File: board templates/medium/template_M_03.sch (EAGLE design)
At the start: 2 parts

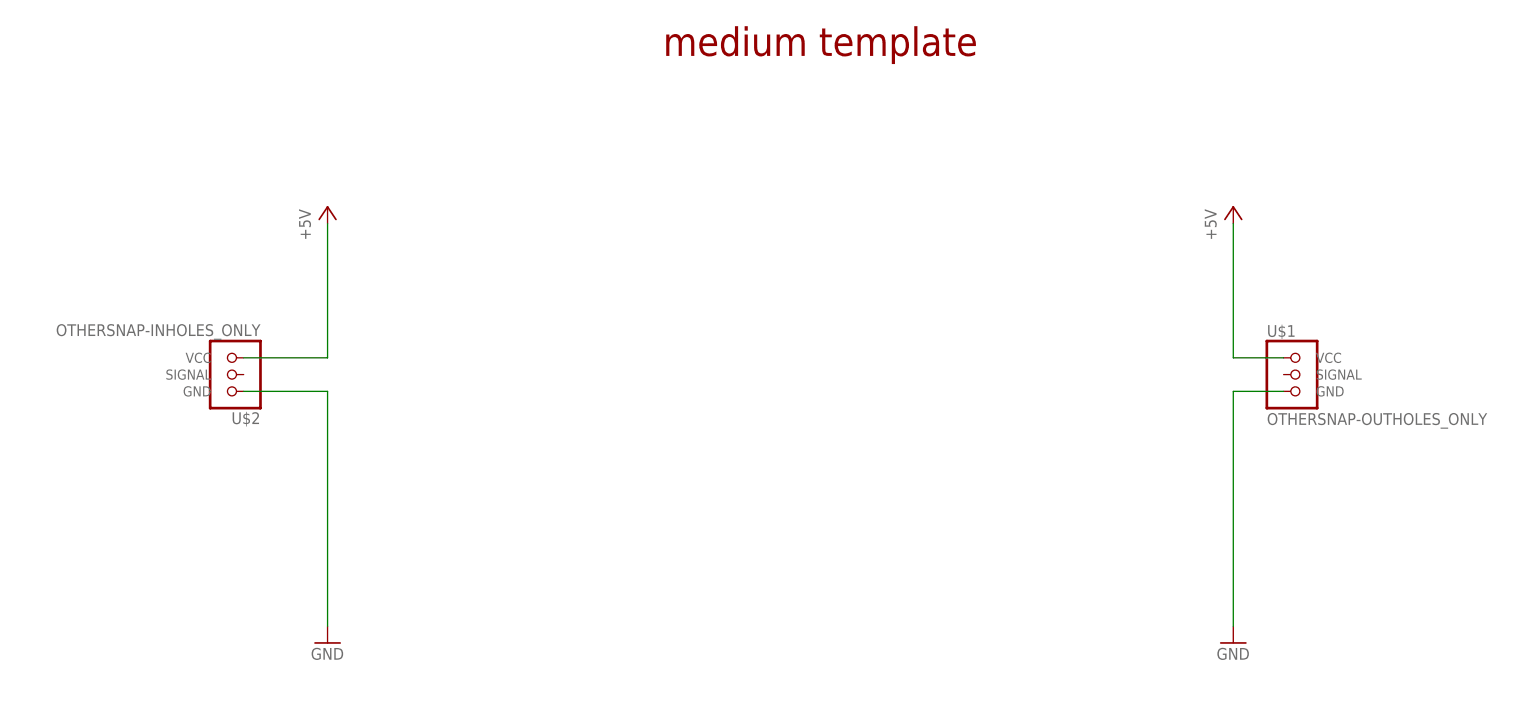
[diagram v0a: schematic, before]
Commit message: standard grid sizes on brd templates
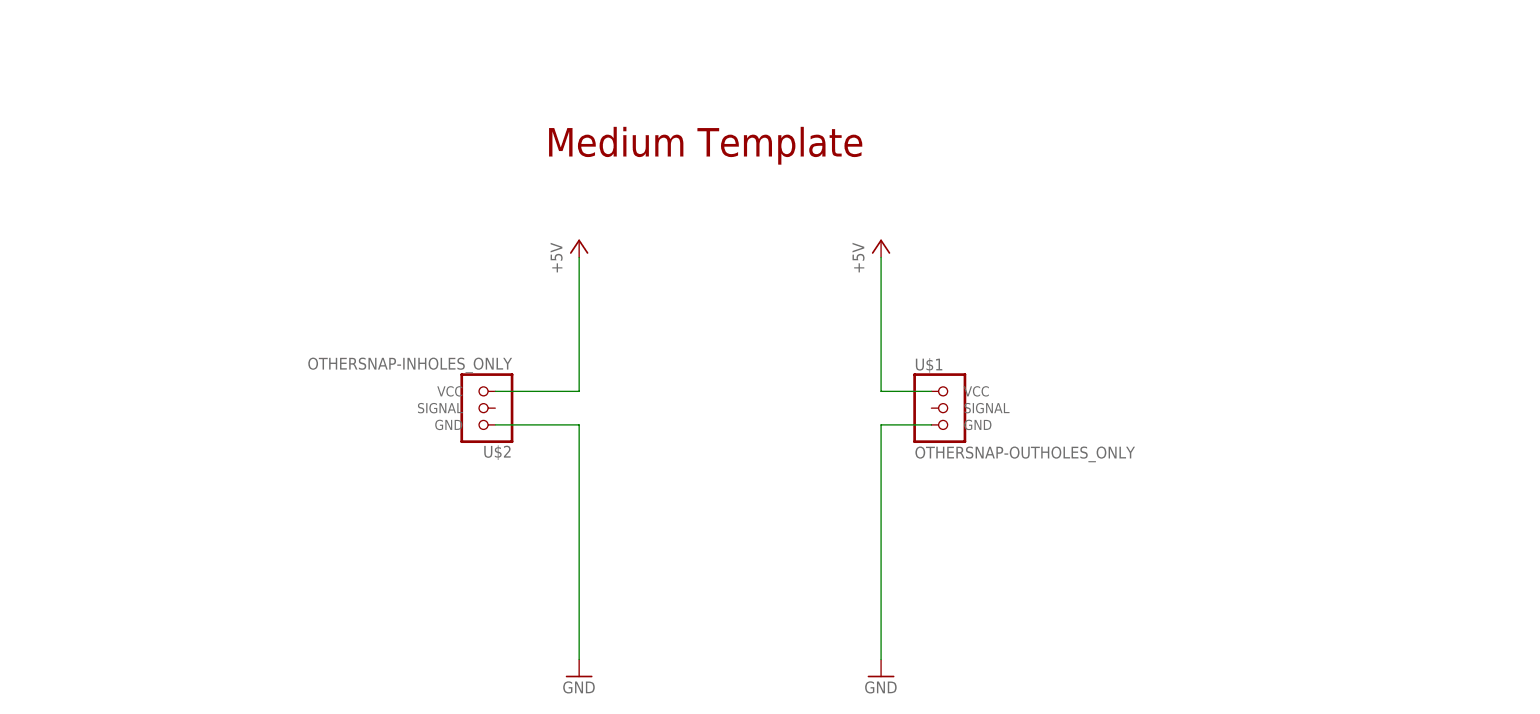
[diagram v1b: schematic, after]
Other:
- note added: "Medium Template"
- note removed: "medium template"
- moved on the sheet: U$1, U$2
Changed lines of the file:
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@@
 <grid distance="0.1" unitdist="inch" unit="inch" style="lines" multiple="1" display="no" altdistance="0.01" altunitdist="inch" altunit="inch"/>
 <layers>
-<layer number="1" name="Top" color="4" fill="1" visible="yes" active="no"/>
-<layer number="16" name="Bottom" color="1" fill="1" visible="yes" active="no"/>
-<layer number="17" name="Pads" color="2" fill="1" visible="yes" active="no"/>
-<layer number="18" name="Vias" color="2" fill="1" visible="yes" active="no"/>
-<layer number="19" name="Unrouted" color="6" fill="1" visible="yes" active="no"/>
-<layer number="20" name="Dimension" color="15" fill="1" visible="yes" active="no"/>
-<layer number="21" name="tPlace" color="7" fill="1" visible="yes" active="no"/>
-<layer number="22" name="bPlace" color="7" fill="1" visible="yes" active="no"/>
-<layer number="23" name="tOrigins" color="15" fill="1" visible="yes" active="no"/>
-<layer number="24" name="bOrigins" color="15" fill="1" visible="yes" active="no"/>
-<layer number="25" name="tNames" color="7" fill="1" visible="yes" active="no"/>
-<layer number="26" name="bNames" color="7" fill="1" visible="yes" active="no"/>
-<layer number="27" name="tValues" color="7" fill="1" visible="yes" active="no"/>
-<layer number="28" name="bValues" color="7" fill="1" visible="yes" active="no"/>
+<layer number="1" name="Top" color="4" fill="1" visible="no" active="no"/>
+<layer number="16" name="Bottom" color="1" fill="1" visible="no" active="no"/>
+<layer number="17" name="Pads" color="2" fill="1" visible="no" active="no"/>
+<layer number="18" name="Vias" color="2" fill="1" visible="no" active="no"/>
+<layer number="19" name="Unrouted" color="6" fill="1" visible="no" active="no"/>
+<layer number="20" name="Dimension" color="15" fill="1" visible="no" active="no"/>
+<layer number="21" name="tPlace" color="7" fill="1" visible="no" active="no"/>
+<layer number="22" name="bPlace" color="7" fill="1" visible="no" active="no"/>
+<layer number="23" name="tOrigins" color="15" fill="1" visible="no" active="no"/>
+<layer number="24" name="bOrigins" color="15" fill="1" visible="no" active="no"/>
+<layer number="25" name="tNames" color="7" fill="1" visible="no" active="no"/>
+<layer number="26" name="bNames" color="7" fill="1" visible="no" active="no"/>
+<layer number="27" name="tValues" color="7" fill="1" visible="no" active="no"/>
+<layer number="28" name="bValues" color="7" fill="1" visible="no" active="no"/>
 <layer number="29" name="tStop" color="7" fill="3" visible="no" active="no"/>
 <layer number="30" name="bStop" color="7" fill="6" visible="no" active="no"/>
@@
 <layer number="35" name="tGlue" color="7" fill="4" visible="no" active="no"/>
 <layer number="36" name="bGlue" color="7" fill="5" visible="no" active="no"/>
-<layer number="37" name="tTest" color="7" fill="1" visible="yes" active="no"/>
-<layer number="38" name="bTest" color="7" fill="1" visible="yes" active="no"/>
+<layer number="37" name="tTest" color="7" fill="1" visible="no" active="no"/>
+<layer number="38" name="bTest" color="7" fill="1" visible="no" active="no"/>
 <layer number="39" name="tKeepout" color="4" fill="11" visible="no" active="no"/>
 <layer number="40" name="bKeepout" color="1" fill="11" visible="no" active="no"/>
@@
 <layer number="44" name="Drills" color="7" fill="1" visible="no" active="no"/>
 <layer number="45" name="Holes" color="7" fill="1" visible="no" active="no"/>
-<layer number="46" name="Milling" color="3" fill="1" visible="yes" active="no"/>
-<layer number="47" name="Measures" color="7" fill="1" visible="yes" active="no"/>
-<layer number="48" name="Document" color="7" fill="1" visible="yes" active="no"/>
-<layer number="49" name="Reference" color="7" fill="1" visible="yes" active="no"/>
-<layer number="50" name="dxf" color="7" fill="1" visible="yes" active="no"/>
-<layer number="51" name="tDocu" color="7" fill="1" visible="yes" active="no"/>
-<layer number="52" name="bDocu" color="7" fill="1" visible="yes" active="no"/>
-<layer number="53" name="tGND_GNDA" color="7" fill="9" visible="yes" active="no"/>
-<layer number="54" name="bGND_GNDA" color="1" fill="9" visible="yes" active="no"/>
-<layer number="56" name="wert" color="7" fill="1" visible="yes" active="no"/>
-<layer number="57" name="tCAD" color="7" fill="1" visible="yes" active="no"/>
-<layer number="59" name="tCarbon" color="7" fill="1" visible="yes" active="no"/>
-<layer number="60" name="bCarbon" color="7" fill="1" visible="yes" active="no"/>
+<layer number="46" name="Milling" color="3" fill="1" visible="no" active="no"/>
+<layer number="47" name="Measures" color="7" fill="1" visible="no" active="no"/>
+<layer number="48" name="Document" color="7" fill="1" visible="no" active="no"/>
+<layer number="49" name="Reference" color="7" fill="1" visible="no" active="no"/>
+<layer number="50" name="dxf" color="7" fill="1" visible="no" active="no"/>
+<layer number="51" name="tDocu" color="7" fill="1" visible="no" active="no"/>
+<layer number="52" name="bDocu" color="7" fill="1" visible="no" active="no"/>
+<layer number="53" name="tGND_GNDA" color="7" fill="9" visible="no" active="no"/>
+<layer number="54" name="bGND_GNDA" color="1" fill="9" visible="no" active="no"/>
+<layer number="56" name="wert" color="7" fill="1" visible="no" active="no"/>
+<layer number="57" name="tCAD" color="7" fill="1" visible="no" active="no"/>
+<layer number="59" name="tCarbon" color="7" fill="1" visible="no" active="no"/>
+<layer number="60" name="bCarbon" color="7" fill="1" visible="no" active="no"/>
 <layer number="90" name="Modules" color="5" fill="1" visible="yes" active="yes"/>
 <layer number="91" name="Nets" color="2" fill="1" visible="yes" active="yes"/>
@@
 <sheet>
 <plain>
-<text x="132.08" y="170.18" size="4.318" layer="94" font="vector">medium template</text>
+<text x="114.3" y="154.94" size="4.318" layer="94" font="vector">Medium Template</text>
 </plain>
 <instances>
 <instance part="FRAME1" gate="G$1" x="0" y="0"/>
 <instance part="FRAME1" gate="G$2" x="172.72" y="0"/>
-<instance part="GND3" gate="1" x="81.28" y="81.28"/>
-<instance part="U$1" gate="G$1" x="228.6" y="121.92"/>
-<instance part="GND5" gate="1" x="218.44" y="81.28"/>
-<instance part="U$2" gate="G$1" x="66.04" y="121.92"/>
-<instance part="P+1" gate="1" x="81.28" y="147.32"/>
-<instance part="P+2" gate="1" x="218.44" y="147.32"/>
+<instance part="GND3" gate="1" x="119.38" y="76.2"/>
+<instance part="U$1" gate="G$1" x="175.26" y="116.84"/>
+<instance part="GND5" gate="1" x="165.1" y="76.2"/>
+<instance part="U$2" gate="G$1" x="104.14" y="116.84"/>
+<instance part="P+1" gate="1" x="119.38" y="142.24"/>
+<instance part="P+2" gate="1" x="165.1" y="142.24"/>
 </instances>
 <busses>
@@
 <net name="GND" class="0">
 <segment>
-<wire x1="81.28" y1="119.38" x2="81.28" y2="83.82" width="0.1524" layer="91"/>
+<wire x1="119.38" y1="114.3" x2="119.38" y2="78.74" width="0.1524" layer="91"/>
 <pinref part="GND3" gate="1" pin="GND"/>
 <pinref part="U$2" gate="G$1" pin="GND"/>
-<wire x1="68.58" y1="119.38" x2="81.28" y2="119.38" width="0.1524" layer="91"/>
+<wire x1="106.68" y1="114.3" x2="119.38" y2="114.3" width="0.1524" layer="91"/>
 </segment>
 <segment>
 <pinref part="U$1" gate="G$1" pin="GND"/>
-<wire x1="226.06" y1="119.38" x2="218.44" y2="119.38" width="0.1524" layer="91"/>
-<wire x1="218.44" y1="119.38" x2="218.44" y2="83.82" width="0.1524" layer="91"/>
+<wire x1="172.72" y1="114.3" x2="165.1" y2="114.3" width="0.1524" layer="91"/>
+<wire x1="165.1" y1="114.3" x2="165.1" y2="78.74" width="0.1524" layer="91"/>
 <pinref part="GND5" gate="1" pin="GND"/>
 </segment>
@@
 <pinref part="U$2" gate="G$1" pin="VCC"/>
 <pinref part="P+1" gate="1" pin="+5V"/>
-<wire x1="68.58" y1="124.46" x2="81.28" y2="124.46" width="0.1524" layer="91"/>
-<wire x1="81.28" y1="124.46" x2="81.28" y2="144.78" width="0.1524" layer="91"/>
+<wire x1="106.68" y1="119.38" x2="119.38" y2="119.38" width="0.1524" layer="91"/>
+<wire x1="119.38" y1="119.38" x2="119.38" y2="139.7" width="0.1524" layer="91"/>
 </segment>
 <segment>
 <pinref part="P+2" gate="1" pin="+5V"/>
-<wire x1="218.44" y1="144.78" x2="218.44" y2="124.46" width="0.1524" layer="91"/>
+<wire x1="165.1" y1="139.7" x2="165.1" y2="119.38" width="0.1524" layer="91"/>
 <pinref part="U$1" gate="G$1" pin="VCC"/>
-<wire x1="218.44" y1="124.46" x2="226.06" y2="124.46" width="0.1524" layer="91"/>
+<wire x1="165.1" y1="119.38" x2="172.72" y2="119.38" width="0.1524" layer="91"/>
 </segment>
 </net>
